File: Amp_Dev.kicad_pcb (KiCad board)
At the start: 2 copper layers, 100 x 100 mm, 511 parts, among them J1 SMA, J10 SMA, J11 CONN_01X02, J12 TEST_1P, J13 SMA, J14 CONN_01X02, J15 CONN_01X03, J16 TEST_1P, J17 TEST_1P, J18 TEST_1P, J2 SMA, J20 SMA, J21 SMA, J22 SMA, J3 TEST_1P, J4 TEST_1P, J5 CONN_01X03, J6 TEST_1P, J7 CONN_01X03, J8 TEST_1P, J9 TEST_1P, Q1 DMN2075U, U1 MML09211H, U2 RF6886, U3 LMV358, U4 SN74LVC1G17, U5 TLV702, U6 LTC2644, U7 RT9183

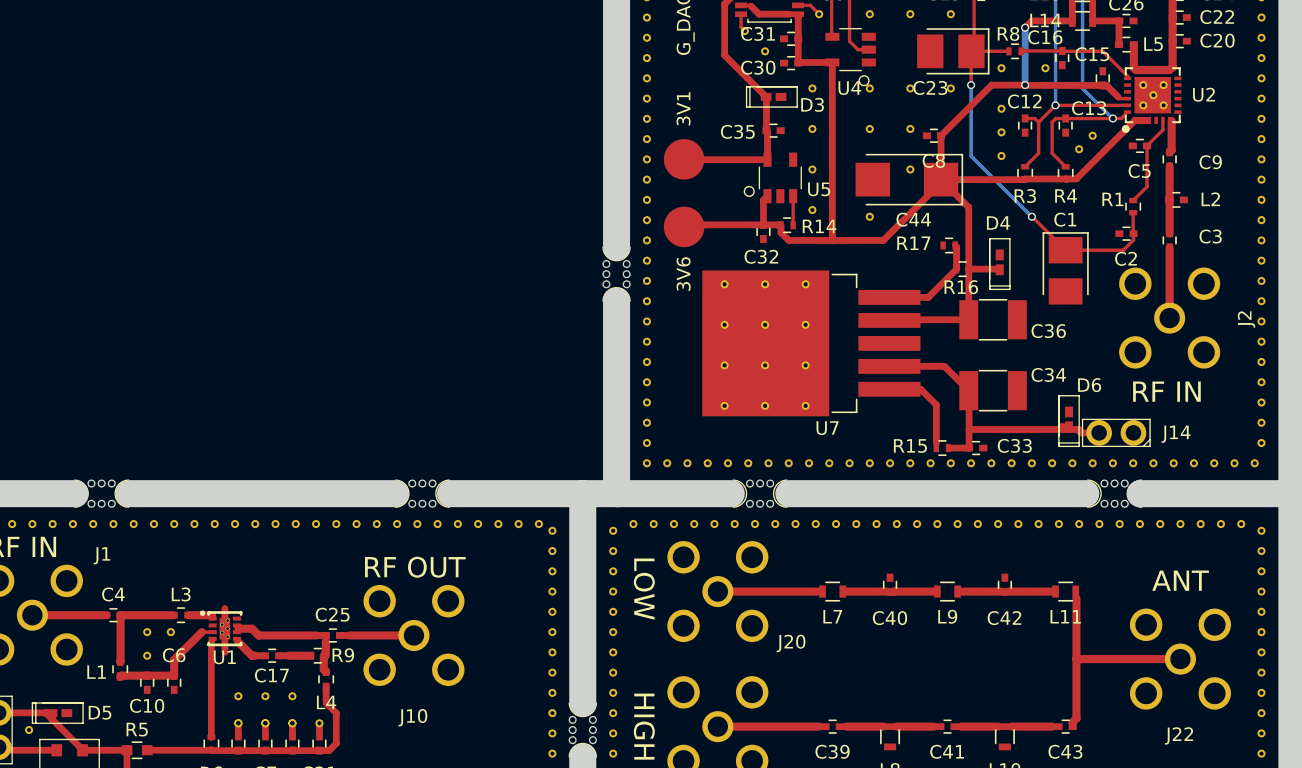
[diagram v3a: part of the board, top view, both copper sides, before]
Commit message: moved L1 closer to RF path
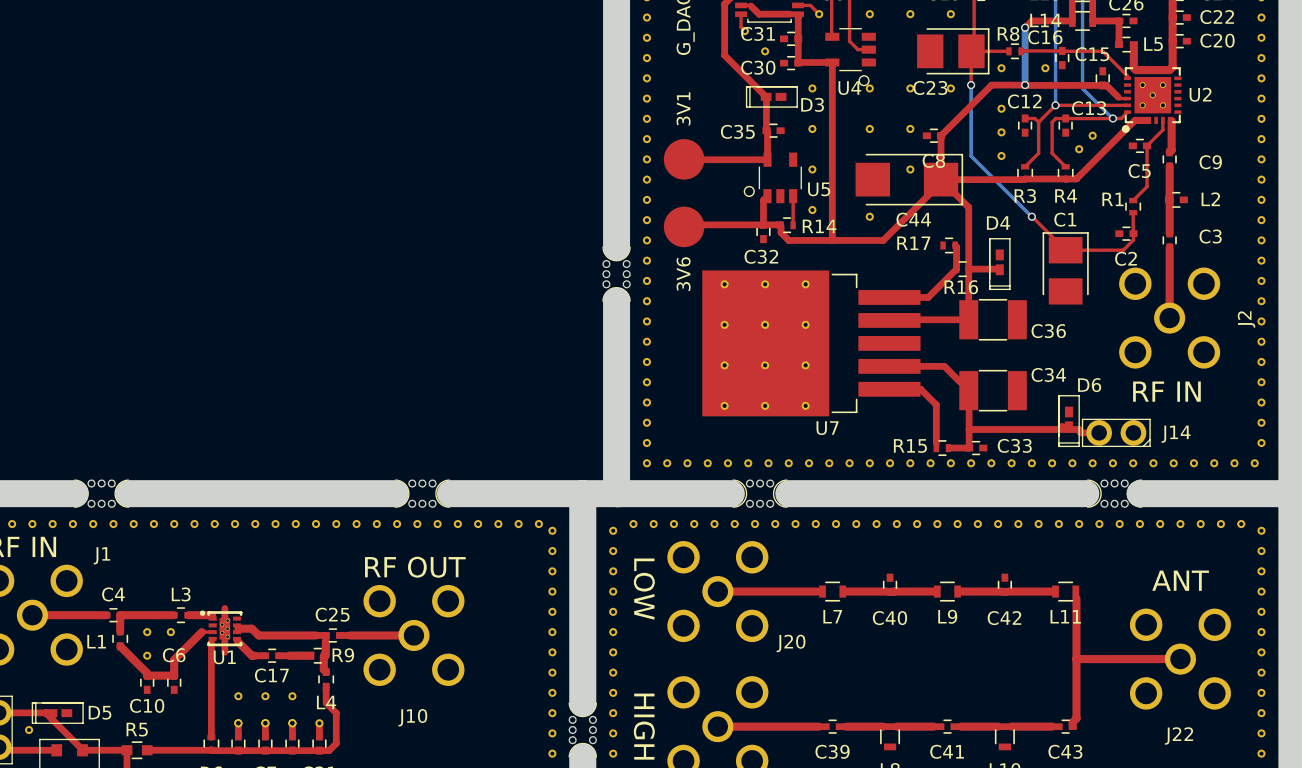
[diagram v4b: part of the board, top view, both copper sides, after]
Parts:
- removed the REF** at (189.0, 84.8)
- removed the REF** at (189.0, 86.2)
- removed the REF** at (190.5, 86.2)
- removed the REF** at (190.5, 84.8)
- removed the REF** at (189.8, 85.5)
- moved L1 2.25 mm to (113.2, 125.8)
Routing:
- net Net-(C4-Pad1): track 7.39 -> 5.14 mm
- net Net-(C10-Pad1): track 8.91 -> 9.88 mm

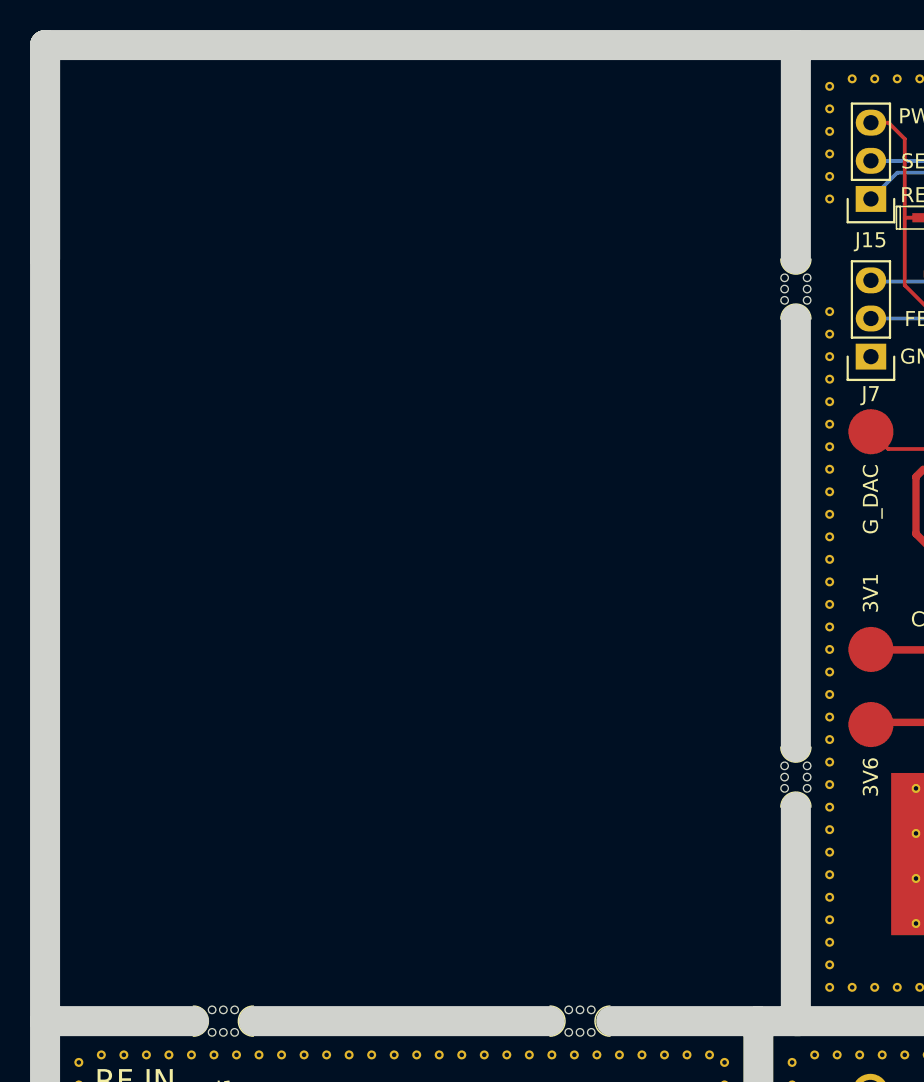
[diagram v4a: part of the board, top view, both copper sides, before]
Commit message: Duplicated PA board
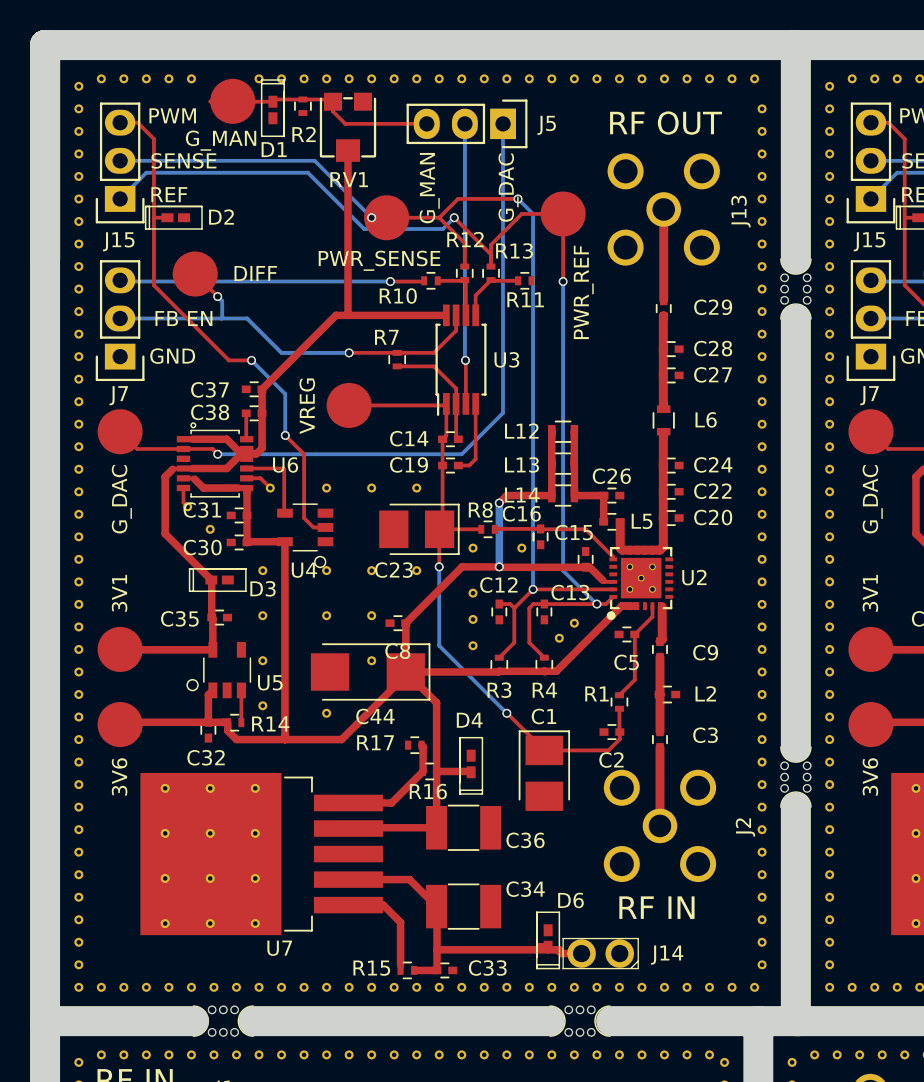
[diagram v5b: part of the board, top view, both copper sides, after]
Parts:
- added C1: 10uF, SFUSat:CP_Tantalum_Case-B_EIA-1411-21_Reflow, F.Cu at (133.2, 98.5)
- added C12: 1uF, SFUSat:C_0402, F.Cu at (130.2, 87.8)
- added C13: 1uF, SFUSat:C_0402, F.Cu at (133.2, 87.8)
- added C14: 0.1uF, SFUSat:C_0402, F.Cu at (127.0, 76.2)
- added C15: 1uF, SFUSat:C_0402, F.Cu at (136.0, 84.2)
- added C16: 2.2uF, SFUSat:C_0402, F.Cu at (133.0, 82.8)
- added C19: 1uF, SFUSat:C_0402, F.Cu at (127.0, 78.0)
- added C2: 1uF, SFUSat:C_0402, F.Cu at (137.8, 95.8)
- added C20: DNP, SFUSat:C_0402, F.Cu at (141.7, 81.5)
- added C22: 10pF, SFUSat:C_0402, F.Cu at (141.7, 79.8)
- added C23: 10uF, SFUSat:CP_Tantalum_Case-B_EIA-1411-21_Reflow, F.Cu at (124.8, 82.2)
- added C24: 27pF, SFUSat:C_0402, F.Cu at (141.7, 78.0)
- added C26: 2.2uF, SFUSat:C_0402, F.Cu at (137.8, 80.0)
- added C27: 10pF, SFUSat:C_0402, F.Cu at (141.7, 72.0)
- added C28: 1.2pF, SFUSat:C_0402, F.Cu at (141.7, 70.2)
- added C29: 100pF, SFUSat:C_0402, F.Cu at (141.2, 67.5)
- added C3: 100pF, SFUSat:C_0402, F.Cu at (140.9, 96.2)
- added C30: 0.1uF, SFUSat:C_0402, F.Cu at (112.9, 83.1)
- added C31: 0.1uF, SFUSat:C_0402, F.Cu at (112.9, 81.3)
- added C32: 1uF, SFUSat:C_0402, F.Cu at (110.9, 95.6)
- added C33: 0.1uF, SFUSat:C_0402, F.Cu at (126.6, 111.6)
- added C34: 10uF, SFUSat:C_1210, F.Cu at (127.9, 107.4)
- added C35: 1uF, SFUSat:C_0402, F.Cu at (111.6, 88.1)
- added C36: 10uF, SFUSat:C_1210, F.Cu at (127.9, 102.1)
- added C37: 0.1uF, SFUSat:C_0402, F.Cu at (113.9, 72.9)
- added C38: 0.1uF, SFUSat:C_0402, F.Cu at (113.9, 74.5)
- added C44: 10uF, SFUSat:CP_Tantalum_Case-C_EIA-2312-28_Reflow, F.Cu at (121.5, 91.8)
- added C5: 2.2uF, SFUSat:C_0402, F.Cu at (138.8, 89.2)
- added C8: 220pF, SFUSat:C_0402, F.Cu at (123.5, 88.5)
- added C9: 22pF, SFUSat:C_0402, F.Cu at (140.9, 90.2)
- added D1: PESD5Zx, SFUSat:PESD57zx, F.Cu at (115.2, 54.3)
- added D2: PESD5Zx, SFUSat:PESD57zx, F.Cu at (108.7, 61.5)
- added D3: PESD5Zx, SFUSat:PESD57zx, F.Cu at (111.6, 85.6)
- added D4: PESD5Zx, SFUSat:PESD57zx, F.Cu at (128.4, 97.9)
- added D6: PESD5Zx, SFUSat:PESD57zx, F.Cu at (133.5, 109.5)
- added G***: LOGO, SFUSat:SFUSat_15mm_2, B.Cu at (107.8, 105.8)
- added J13: SMA, SFUSat:SMA-Vert-TH, F.Cu at (141.2, 61.0)
- added J14: CONN_01X02, SFUSat:2x01In_Header_v2, F.Cu at (137.0, 110.5)
- added J15: CONN_01X03, SFUSat:Socket_Strip_Straight_1x03, F.Cu at (105.0, 60.2)
- added J16: TEST_1P, SFUSat:Measurement_Point_Round-SMD-Pad_Big, F.Cu at (105.0, 90.2)
- added J17: TEST_1P, SFUSat:Measurement_Point_Round-SMD-Pad_Big, F.Cu at (105.0, 95.2)
- added J18: TEST_1P, SFUSat:Measurement_Point_Round-SMD-Pad_Big, F.Cu at (105.0, 75.8)
- added J2: SMA, SFUSat:SMA-Vert-TH, F.Cu at (140.9, 102.0)
- added J3: TEST_1P, SFUSat:Measurement_Point_Round-SMD-Pad_Big, F.Cu at (112.5, 53.8)
- added J4: TEST_1P, SFUSat:Measurement_Point_Round-SMD-Pad_Big, F.Cu at (120.2, 74.0)
- added J5: CONN_01X03, SFUSat:Socket_Strip_Straight_1x03, F.Cu at (130.5, 55.2)
- added J6: TEST_1P, SFUSat:Measurement_Point_Round-SMD-Pad_Big, F.Cu at (110.0, 65.2)
- added J7: CONN_01X03, SFUSat:Socket_Strip_Straight_1x03, F.Cu at (105.0, 70.8)
- added J8: TEST_1P, SFUSat:Measurement_Point_Round-SMD-Pad_Big, F.Cu at (122.8, 61.5)
- added J9: TEST_1P, SFUSat:Measurement_Point_Round-SMD-Pad_Big, F.Cu at (134.5, 61.2)
- added L12: 0R0, SFUSat:L_0603, F.Cu at (134.5, 75.8)
- added L13: 0R0, SFUSat:L_0603, F.Cu at (134.5, 77.9)
- added L14: 0R0, SFUSat:L_0603, F.Cu at (134.5, 80.0)
- added L2: 8.2nH, SFUSat:L_0402, F.Cu at (141.4, 93.2)
- added L5: 12.55nH, SFUSat:L_0402, F.Cu at (137.8, 81.8)
- added L6: 0R0, SFUSat:L_0603, F.Cu at (141.2, 75.0)
- added R1: 220R, SFUSat:R_0402, F.Cu at (138.2, 93.8)
- added R10: 10K, SFUSat:R_0402, F.Cu at (125.7, 65.7)
- added R11: 10K, SFUSat:R_0402, F.Cu at (131.9, 65.7)
- added R12: 10K, SFUSat:R_0402, F.Cu at (128.0, 65.2)
- added R13: 10K, SFUSat:R_0402, F.Cu at (129.7, 65.2)
- added R14: 1K, SFUSat:R_0402, F.Cu at (112.6, 95.1)
- added R15: 1k, SFUSat:R_0402, F.Cu at (124.1, 111.6)
- added R16: 1k, SFUSat:R_0402, F.Cu at (125.6, 98.4)
- added R17: 287R, SFUSat:R_0402, F.Cu at (124.6, 96.6)
- added R2: 1K, SFUSat:R_0402, F.Cu at (117.2, 54.1)
- added R3: 390R, SFUSat:R_0402, F.Cu at (130.2, 91.2)
- added R4: 390R, SFUSat:R_0402, F.Cu at (133.2, 91.2)
- added R7: 1K, SFUSat:R_0402, F.Cu at (123.5, 71.0)
- added R8: 220R, SFUSat:R_0402, F.Cu at (129.5, 82.2)
- added REF**: VIA-0.6mm, SFUSat:VIA-0.6mm, F.Cu at (152.2, 66.2)
- added REF**: VIA-0.6mm, SFUSat:VIA-0.6mm, F.Cu at (115.0, 79.5)
- added REF**: VIA-0.6mm, SFUSat:VIA-0.6mm, F.Cu at (147.8, 78.2)
- added REF**: VIA-0.6mm, SFUSat:VIA-0.6mm, F.Cu at (147.8, 76.8)
- added REF**: VIA-0.6mm, SFUSat:VIA-0.6mm, F.Cu at (147.8, 75.2)
- added REF**: VIA-0.6mm, SFUSat:VIA-0.6mm, F.Cu at (147.8, 73.8)
- added REF**: VIA-0.6mm, SFUSat:VIA-0.6mm, F.Cu at (147.8, 72.2)
- added REF**: VIA-0.6mm, SFUSat:VIA-0.6mm, F.Cu at (147.8, 70.8)
- added REF**: VIA-0.6mm, SFUSat:VIA-0.6mm, F.Cu at (147.8, 69.2)
- added REF**: VIA-0.6mm, SFUSat:VIA-0.6mm, F.Cu at (147.8, 67.8)
- added REF**: VIA-0.6mm, SFUSat:VIA-0.6mm, F.Cu at (147.8, 66.2)
- added REF**: VIA-0.6mm, SFUSat:VIA-0.6mm, F.Cu at (147.8, 64.8)
- added REF**: VIA-0.6mm, SFUSat:VIA-0.6mm, F.Cu at (102.2, 112.8)
- added REF**: VIA-0.6mm, SFUSat:VIA-0.6mm, F.Cu at (147.8, 63.2)
- added REF**: VIA-0.6mm, SFUSat:VIA-0.6mm, F.Cu at (147.8, 61.8)
- added REF**: VIA-0.6mm, SFUSat:VIA-0.6mm, F.Cu at (147.8, 60.2)
- added REF**: VIA-0.6mm, SFUSat:VIA-0.6mm, F.Cu at (147.8, 58.8)
- added REF**: VIA-0.6mm, SFUSat:VIA-0.6mm, F.Cu at (147.8, 57.2)
- added REF**: VIA-0.6mm, SFUSat:VIA-0.6mm, F.Cu at (147.8, 55.8)
- added REF**: VIA-0.6mm, SFUSat:VIA-0.6mm, F.Cu at (147.8, 54.2)
- added REF**: VIA-0.6mm, SFUSat:VIA-0.6mm, F.Cu at (103.8, 52.2)
- added REF**: VIA-0.6mm, SFUSat:VIA-0.6mm, F.Cu at (105.2, 52.2)
- added REF**: VIA-0.6mm, SFUSat:VIA-0.6mm, F.Cu at (106.8, 52.2)
- added REF**: VIA-0.6mm, SFUSat:VIA-0.6mm, F.Cu at (102.2, 111.2)
- added REF**: VIA-0.6mm, SFUSat:VIA-0.6mm, F.Cu at (108.2, 52.2)
- added REF**: VIA-0.6mm, SFUSat:VIA-0.6mm, F.Cu at (109.8, 52.2)
- added REF**: VIA-0.6mm, SFUSat:VIA-0.6mm, F.Cu at (114.2, 52.2)
- added REF**: VIA-0.6mm, SFUSat:VIA-0.6mm, F.Cu at (115.8, 52.2)
- added REF**: VIA-0.6mm, SFUSat:VIA-0.6mm, F.Cu at (117.2, 52.2)
- added REF**: VIA-0.6mm, SFUSat:VIA-0.6mm, F.Cu at (118.8, 52.2)
- added REF**: VIA-0.6mm, SFUSat:VIA-0.6mm, F.Cu at (120.2, 52.2)
- added REF**: VIA-0.6mm, SFUSat:VIA-0.6mm, F.Cu at (121.8, 52.2)
- added REF**: VIA-0.6mm, SFUSat:VIA-0.6mm, F.Cu at (123.2, 52.2)
- added REF**: VIA-0.6mm, SFUSat:VIA-0.6mm, F.Cu at (124.8, 52.2)
- added REF**: VIA-0.6mm, SFUSat:VIA-0.6mm, F.Cu at (102.2, 109.8)
- added REF**: VIA-0.6mm, SFUSat:VIA-0.6mm, F.Cu at (126.2, 52.2)
- added REF**: VIA-0.6mm, SFUSat:VIA-0.6mm, F.Cu at (127.8, 52.2)
- added REF**: VIA-0.6mm, SFUSat:VIA-0.6mm, F.Cu at (129.2, 52.2)
- added REF**: VIA-0.6mm, SFUSat:VIA-0.6mm, F.Cu at (130.8, 52.2)
- added REF**: VIA-0.6mm, SFUSat:VIA-0.6mm, F.Cu at (132.2, 52.2)
- added REF**: VIA-0.6mm, SFUSat:VIA-0.6mm, F.Cu at (133.8, 52.2)
- added REF**: VIA-0.6mm, SFUSat:VIA-0.6mm, F.Cu at (135.2, 52.2)
- added REF**: VIA-0.6mm, SFUSat:VIA-0.6mm, F.Cu at (136.8, 52.2)
- added REF**: VIA-0.6mm, SFUSat:VIA-0.6mm, F.Cu at (138.2, 52.2)
- added REF**: VIA-0.6mm, SFUSat:VIA-0.6mm, F.Cu at (139.8, 52.2)
- added REF**: VIA-0.6mm, SFUSat:VIA-0.6mm, F.Cu at (102.2, 108.2)
- added REF**: VIA-0.6mm, SFUSat:VIA-0.6mm, F.Cu at (141.2, 52.2)
- added REF**: VIA-0.6mm, SFUSat:VIA-0.6mm, F.Cu at (142.8, 52.2)
- added REF**: VIA-0.6mm, SFUSat:VIA-0.6mm, F.Cu at (144.2, 52.2)
- added REF**: VIA-0.6mm, SFUSat:VIA-0.6mm, F.Cu at (145.8, 52.2)
- added REF**: VIA-0.6mm, SFUSat:VIA-0.6mm, F.Cu at (147.2, 52.2)
- added REF**: VIA-0.6mm, SFUSat:VIA-0.6mm, F.Cu at (128.5, 90.0)
- added REF**: VIA-0.6mm, SFUSat:VIA-0.6mm, F.Cu at (128.5, 88.2)
- added REF**: VIA-0.6mm, SFUSat:VIA-0.6mm, F.Cu at (128.5, 86.5)
- added REF**: VIA-0.6mm, SFUSat:VIA-0.6mm, F.Cu at (134.2, 89.5)
- added REF**: VIA-0.6mm, SFUSat:VIA-0.6mm, F.Cu at (128.5, 83.5)
- added REF**: VIA-0.6mm, SFUSat:VIA-0.6mm, F.Cu at (102.2, 106.8)
- added REF**: VIA-0.6mm, SFUSat:VIA-0.6mm, F.Cu at (131.8, 83.5)
- added REF**: VIA-0.6mm, SFUSat:VIA-0.6mm, F.Cu at (108.0, 99.5)
- added REF**: VIA-0.6mm, SFUSat:VIA-0.6mm, F.Cu at (111.0, 99.5)
- added REF**: VIA-0.6mm, SFUSat:VIA-0.6mm, F.Cu at (114.0, 99.5)
- added REF**: VIA-0.6mm, SFUSat:VIA-0.6mm, F.Cu at (108.0, 102.5)
- added REF**: VIA-0.6mm, SFUSat:VIA-0.6mm, F.Cu at (111.0, 102.5)
- added REF**: VIA-0.6mm, SFUSat:VIA-0.6mm, F.Cu at (114.0, 102.5)
- added REF**: VIA-0.6mm, SFUSat:VIA-0.6mm, F.Cu at (108.0, 105.5)
- added REF**: VIA-0.6mm, SFUSat:VIA-0.6mm, F.Cu at (111.0, 105.5)
- added REF**: VIA-0.6mm, SFUSat:VIA-0.6mm, F.Cu at (114.0, 105.5)
- added REF**: VIA-0.6mm, SFUSat:VIA-0.6mm, F.Cu at (102.2, 105.2)
- added REF**: VIA-0.6mm, SFUSat:VIA-0.6mm, F.Cu at (108.0, 108.5)
- added REF**: VIA-0.6mm, SFUSat:VIA-0.6mm, F.Cu at (111.0, 108.5)
- added REF**: VIA-0.6mm, SFUSat:VIA-0.6mm, F.Cu at (114.0, 108.5)
- added REF**: VIA-0.6mm, SFUSat:VIA-0.6mm, F.Cu at (109.5, 80.8)
- added REF**: VIA-0.6mm, SFUSat:VIA-0.6mm, F.Cu at (118.8, 79.5)
- added REF**: VIA-0.6mm, SFUSat:VIA-0.6mm, F.Cu at (121.8, 79.5)
- added REF**: VIA-0.6mm, SFUSat:VIA-0.6mm, F.Cu at (124.8, 79.5)
- added REF**: VIA-0.6mm, SFUSat:VIA-0.6mm, F.Cu at (118.8, 85.0)
- added REF**: VIA-0.6mm, SFUSat:VIA-0.6mm, F.Cu at (124.8, 85.0)
- added REF**: VIA-0.6mm, SFUSat:VIA-0.6mm, F.Cu at (121.8, 85.0)
- added REF**: VIA-0.6mm, SFUSat:VIA-0.6mm, F.Cu at (102.2, 103.8)
- added REF**: VIA-0.6mm, SFUSat:VIA-0.6mm, F.Cu at (118.8, 88.0)
- added REF**: VIA-0.6mm, SFUSat:VIA-0.6mm, F.Cu at (121.8, 88.0)
- added REF**: VIA-0.6mm, SFUSat:VIA-0.6mm, F.Cu at (118.8, 94.5)
- added REF**: VIA-0.6mm, SFUSat:VIA-0.6mm, F.Cu at (121.8, 91.0)
- added REF**: VIA-0.6mm, SFUSat:VIA-0.6mm, F.Cu at (111.0, 82.2)
- added REF**: VIA-0.6mm, SFUSat:VIA-0.6mm, F.Cu at (114.5, 85.0)
- added REF**: VIA-0.6mm, SFUSat:VIA-0.6mm, F.Cu at (114.5, 88.0)
- added REF**: VIA-0.6mm, SFUSat:VIA-0.6mm, F.Cu at (114.5, 91.0)
- added REF**: VIA-0.6mm, SFUSat:VIA-0.6mm, F.Cu at (114.5, 94.0)
- added REF**: VIA-0.6mm, SFUSat:VIA-0.6mm, F.Cu at (102.2, 102.2)
- added REF**: VIA-0.6mm, SFUSat:VIA-0.6mm, F.Cu at (102.2, 100.8)
- added REF**: VIA-0.6mm, SFUSat:VIA-0.6mm, F.Cu at (152.2, 64.8)
- added REF**: VIA-0.6mm, SFUSat:VIA-0.6mm, F.Cu at (102.2, 99.2)
- added REF**: VIA-0.6mm, SFUSat:VIA-0.6mm, F.Cu at (102.2, 97.8)
- added REF**: VIA-0.6mm, SFUSat:VIA-0.6mm, F.Cu at (102.2, 96.2)
- added REF**: VIA-0.6mm, SFUSat:VIA-0.6mm, F.Cu at (102.2, 94.8)
- added REF**: VIA-0.6mm, SFUSat:VIA-0.6mm, F.Cu at (102.2, 93.2)
- added REF**: VIA-0.6mm, SFUSat:VIA-0.6mm, F.Cu at (102.2, 91.8)
- added REF**: VIA-0.6mm, SFUSat:VIA-0.6mm, F.Cu at (102.2, 90.2)
- added REF**: VIA-0.6mm, SFUSat:VIA-0.6mm, F.Cu at (102.2, 88.8)
- added REF**: VIA-0.6mm, SFUSat:VIA-0.6mm, F.Cu at (102.2, 87.2)
- added REF**: VIA-0.6mm, SFUSat:VIA-0.6mm, F.Cu at (102.2, 85.8)
- added REF**: VIA-0.6mm, SFUSat:VIA-0.6mm, F.Cu at (152.2, 63.2)
- added REF**: VIA-0.6mm, SFUSat:VIA-0.6mm, F.Cu at (102.2, 84.2)
- added REF**: VIA-0.6mm, SFUSat:VIA-0.6mm, F.Cu at (102.2, 82.8)
- added REF**: VIA-0.6mm, SFUSat:VIA-0.6mm, F.Cu at (102.2, 81.2)
- added REF**: VIA-0.6mm, SFUSat:VIA-0.6mm, F.Cu at (102.2, 79.8)
- added REF**: VIA-0.6mm, SFUSat:VIA-0.6mm, F.Cu at (102.2, 78.2)
- added REF**: VIA-0.6mm, SFUSat:VIA-0.6mm, F.Cu at (102.2, 76.8)
- added REF**: VIA-0.6mm, SFUSat:VIA-0.6mm, F.Cu at (102.2, 75.2)
- added REF**: VIA-0.6mm, SFUSat:VIA-0.6mm, F.Cu at (102.2, 73.8)
- added REF**: VIA-0.6mm, SFUSat:VIA-0.6mm, F.Cu at (102.2, 72.2)
- added REF**: VIA-0.6mm, SFUSat:VIA-0.6mm, F.Cu at (102.2, 70.8)
- added REF**: VIA-0.6mm, SFUSat:VIA-0.6mm, F.Cu at (152.2, 61.8)
- added REF**: VIA-0.6mm, SFUSat:VIA-0.6mm, F.Cu at (102.2, 69.2)
- added REF**: VIA-0.6mm, SFUSat:VIA-0.6mm, F.Cu at (102.2, 67.8)
- added REF**: VIA-0.6mm, SFUSat:VIA-0.6mm, F.Cu at (102.2, 60.2)
- added REF**: VIA-0.6mm, SFUSat:VIA-0.6mm, F.Cu at (102.2, 58.8)
- added REF**: VIA-0.6mm, SFUSat:VIA-0.6mm, F.Cu at (102.2, 57.2)
- added REF**: VIA-0.6mm, SFUSat:VIA-0.6mm, F.Cu at (102.2, 55.8)
- added REF**: VIA-0.6mm, SFUSat:VIA-0.6mm, F.Cu at (102.2, 54.2)
- added REF**: VIA-0.6mm, SFUSat:VIA-0.6mm, F.Cu at (102.2, 52.8)
- added REF**: VIA-0.6mm, SFUSat:VIA-0.6mm, F.Cu at (103.8, 112.8)
- added REF**: VIA-0.6mm, SFUSat:VIA-0.6mm, F.Cu at (105.2, 112.8)
- added REF**: VIA-0.6mm, SFUSat:VIA-0.6mm, F.Cu at (102.2, 66.2)
- added REF**: VIA-0.6mm, SFUSat:VIA-0.6mm, F.Cu at (106.8, 112.8)
- added REF**: VIA-0.6mm, SFUSat:VIA-0.6mm, F.Cu at (108.2, 112.8)
- added REF**: VIA-0.6mm, SFUSat:VIA-0.6mm, F.Cu at (109.8, 112.8)
- added REF**: VIA-0.6mm, SFUSat:VIA-0.6mm, F.Cu at (111.2, 112.8)
- added REF**: VIA-0.6mm, SFUSat:VIA-0.6mm, F.Cu at (112.8, 112.8)
- added REF**: VIA-0.6mm, SFUSat:VIA-0.6mm, F.Cu at (114.2, 112.8)
- added REF**: VIA-0.6mm, SFUSat:VIA-0.6mm, F.Cu at (115.8, 112.8)
- added REF**: VIA-0.6mm, SFUSat:VIA-0.6mm, F.Cu at (117.2, 112.8)
- added REF**: VIA-0.6mm, SFUSat:VIA-0.6mm, F.Cu at (118.8, 112.8)
- added REF**: VIA-0.6mm, SFUSat:VIA-0.6mm, F.Cu at (120.2, 112.8)
- added REF**: VIA-0.6mm, SFUSat:VIA-0.6mm, F.Cu at (102.2, 64.8)
- added REF**: VIA-0.6mm, SFUSat:VIA-0.6mm, F.Cu at (121.8, 112.8)
- added REF**: VIA-0.6mm, SFUSat:VIA-0.6mm, F.Cu at (123.2, 112.8)
- added REF**: VIA-0.6mm, SFUSat:VIA-0.6mm, F.Cu at (124.8, 112.8)
- added REF**: VIA-0.6mm, SFUSat:VIA-0.6mm, F.Cu at (126.2, 112.8)
- added REF**: VIA-0.6mm, SFUSat:VIA-0.6mm, F.Cu at (127.8, 112.8)
- added REF**: VIA-0.6mm, SFUSat:VIA-0.6mm, F.Cu at (129.2, 112.8)
- added REF**: VIA-0.6mm, SFUSat:VIA-0.6mm, F.Cu at (130.8, 112.8)
- added REF**: VIA-0.6mm, SFUSat:VIA-0.6mm, F.Cu at (132.2, 112.8)
- added REF**: VIA-0.6mm, SFUSat:VIA-0.6mm, F.Cu at (133.8, 112.8)
- added REF**: VIA-0.6mm, SFUSat:VIA-0.6mm, F.Cu at (135.2, 112.8)
- added REF**: VIA-0.6mm, SFUSat:VIA-0.6mm, F.Cu at (102.2, 63.2)
- added REF**: VIA-0.6mm, SFUSat:VIA-0.6mm, F.Cu at (136.8, 112.8)
- added REF**: VIA-0.6mm, SFUSat:VIA-0.6mm, F.Cu at (138.2, 112.8)
- added REF**: VIA-0.6mm, SFUSat:VIA-0.6mm, F.Cu at (139.8, 112.8)
- added REF**: VIA-0.6mm, SFUSat:VIA-0.6mm, F.Cu at (141.2, 112.8)
- added REF**: VIA-0.6mm, SFUSat:VIA-0.6mm, F.Cu at (142.8, 112.8)
- added REF**: VIA-0.6mm, SFUSat:VIA-0.6mm, F.Cu at (144.2, 112.8)
- added REF**: VIA-0.6mm, SFUSat:VIA-0.6mm, F.Cu at (145.8, 112.8)
- added REF**: VIA-0.6mm, SFUSat:VIA-0.6mm, F.Cu at (147.2, 112.8)
- added REF**: VIA-0.6mm, SFUSat:VIA-0.6mm, F.Cu at (147.8, 111.2)
- added REF**: VIA-0.6mm, SFUSat:VIA-0.6mm, F.Cu at (147.8, 109.8)
- added REF**: VIA-0.6mm, SFUSat:VIA-0.6mm, F.Cu at (102.2, 61.8)
- added REF**: VIA-0.6mm, SFUSat:VIA-0.6mm, F.Cu at (147.8, 108.2)
- added REF**: VIA-0.6mm, SFUSat:VIA-0.6mm, F.Cu at (147.8, 106.8)
- added REF**: VIA-0.6mm, SFUSat:VIA-0.6mm, F.Cu at (147.8, 105.2)
- added REF**: VIA-0.6mm, SFUSat:VIA-0.6mm, F.Cu at (147.8, 103.8)
- added REF**: VIA-0.6mm, SFUSat:VIA-0.6mm, F.Cu at (147.8, 102.2)
- added REF**: VIA-0.6mm, SFUSat:VIA-0.6mm, F.Cu at (147.8, 100.8)
- added REF**: VIA-0.6mm, SFUSat:VIA-0.6mm, F.Cu at (147.8, 99.2)
- added REF**: VIA-0.6mm, SFUSat:VIA-0.6mm, F.Cu at (147.8, 97.8)
- added REF**: VIA-0.6mm, SFUSat:VIA-0.6mm, F.Cu at (147.8, 96.2)
- added REF**: VIA-0.6mm, SFUSat:VIA-0.6mm, F.Cu at (147.8, 94.8)
- added REF**: VIA-0.6mm, SFUSat:VIA-0.6mm, F.Cu at (135.2, 88.5)
- added REF**: VIA-0.6mm, SFUSat:VIA-0.6mm, F.Cu at (147.8, 93.2)
- added REF**: VIA-0.6mm, SFUSat:VIA-0.6mm, F.Cu at (147.8, 91.8)
- added REF**: VIA-0.6mm, SFUSat:VIA-0.6mm, F.Cu at (147.8, 90.2)
- added REF**: VIA-0.6mm, SFUSat:VIA-0.6mm, F.Cu at (147.8, 88.8)
- added REF**: VIA-0.6mm, SFUSat:VIA-0.6mm, F.Cu at (147.8, 87.2)
- added REF**: VIA-0.6mm, SFUSat:VIA-0.6mm, F.Cu at (147.8, 85.8)
- added REF**: VIA-0.6mm, SFUSat:VIA-0.6mm, F.Cu at (147.8, 84.2)
- added REF**: VIA-0.6mm, SFUSat:VIA-0.6mm, F.Cu at (147.8, 82.8)
- added REF**: VIA-0.6mm, SFUSat:VIA-0.6mm, F.Cu at (147.8, 81.2)
- added REF**: VIA-0.6mm, SFUSat:VIA-0.6mm, F.Cu at (147.8, 79.8)
- added RV1: POT, SFUSat:TC33_SMD, F.Cu at (120.2, 55.6)
- added U2: RF6886, SFUSat:QFN-24, F.Cu at (139.7, 85.5)
- added U3: LMV358, SFUSat:TSSOP-8_4.4x3mm_Pitch0.65mm, F.Cu at (127.7, 71.0)
- added U4: SN74LVC1G17, SFUSat:SOT_23_5, F.Cu at (117.3, 82.1)
- added U5: TLV702, SFUSat:SOT_23_5, F.Cu at (112.1, 91.6)
- added U6: LTC2644, SFUSat:12-TSSOP, F.Cu at (111.3, 77.9)
- added U7: RT9183, SFUSat:TO-263-5Lead, F.Cu at (115.6, 103.9)
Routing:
- net /3V6: track 117.1 -> 234.1 mm, vias 2 -> 4
- net /PWR_REF: track 72.8 -> 145.5 mm, vias 3 -> 6
- net /PWR_SENSE: track 70.9 -> 141.8 mm, vias 3 -> 6
- net /3V1: track 60.7 -> 121.3 mm
- net /G_DAC: track 46.5 -> 93.0 mm, vias 1 -> 2
- net /VREG: track 42.9 -> 85.8 mm, vias 2 -> 4
- net /MCU_PWM: track 35.6 -> 71.1 mm, vias 2 -> 4
- net Net-(J6-Pad1): track 29.5 -> 59.0 mm, vias 2 -> 4
- net Net-(C33-Pad1): track 23.7 -> 47.3 mm
- net Net-(J7-Pad3): track 20.3 -> 40.6 mm, vias 1 -> 2
- net Net-(J5-Pad2): track 18.7 -> 37.4 mm, vias 1 -> 2
- net /G_MAN: track 15.5 -> 31.1 mm
- net Net-(C20-Pad1): track 12.5 -> 24.9 mm
- net GND: track 17.1 -> 27.0 mm
- net Net-(C16-Pad1): track 8.87 -> 17.7 mm
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
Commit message: generated and reviewed gerbers
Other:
- rule pad_to_mask_clearance: 0.2 -> 0

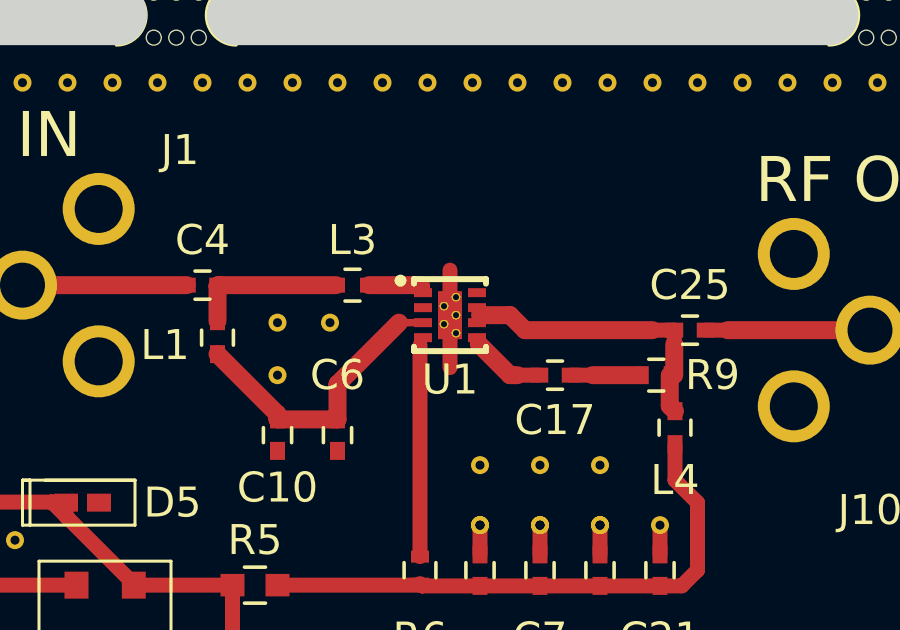
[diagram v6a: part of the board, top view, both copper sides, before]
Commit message: updated LNA footprint to one with 0.3mm drill
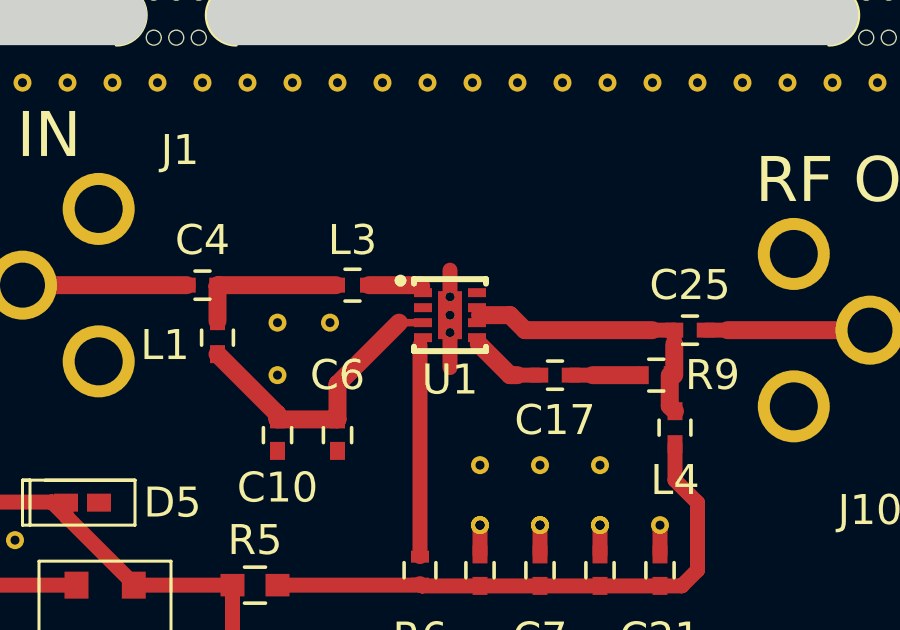
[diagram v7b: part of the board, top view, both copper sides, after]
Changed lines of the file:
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@@
 (kicad_pcb (version 4) (host pcbnew 4.0.6-e0-6349~53~ubuntu16.04.1)
   (general
-    (links 1029)
+    (links 1027)
     (no_connects 44)
     (area 84.435716 48.999999 202.188095 159.700001)
@@
       (net 4 GND) (zone_connect 2))
   )
-  (module SFUSat:8-VFDFN (layer F.Cu)
-    (at 121 125)
-    (fp_text reference U1 (at 0 2.15) (layer F.SilkS)
-      (effects (font (size 1 1) (thickness 0.15)))
-    )
-    (fp_text value MML09211H (at 0 -2) (layer F.Fab)
-      (effects (font (size 1 1) (thickness 0.15)))
-    )
-    (fp_circle (center -1.65 -1.15) (end -1.55 -1.15) (layer F.SilkS) (width 0.2))
-    (fp_line (start -1.2 1.2) (end -1.2 1.05) (layer F.SilkS) (width 0.2))
-    (fp_line (start 1.2 1.2) (end 1.2 1.05) (layer F.SilkS) (width 0.2))
-    (fp_line (start -1.2 1.2) (end 1.15 1.2) (layer F.SilkS) (width 0.2))
-    (fp_line (start 1.15 1.2) (end 1.2 1.2) (layer F.SilkS) (width 0.2))
-    (fp_line (start -1.2 -1.2) (end -1.2 -1.05) (layer F.SilkS) (width 0.2))
-    (fp_line (start -1.2 -1.2) (end 1.2 -1.2) (layer F.SilkS) (width 0.2))
-    (fp_line (start 1.2 -1.2) (end 1.2 -1.05) (layer F.SilkS) (width 0.2))
-    (fp_line (start -1 -1) (end 1 -1) (layer F.Fab) (width 0.2))
-    (fp_line (start 1 -1) (end 1 1) (layer F.Fab) (width 0.2))
-    (fp_line (start 1 1) (end -1 1) (layer F.Fab) (width 0.2))
-    (fp_line (start -1 1) (end -1 -1) (layer F.Fab) (width 0.2))
-    (pad 9 thru_hole circle (at 0.2 -0.6) (size 0.3 0.3) (drill 0.2) (layers *.Cu F.Mask)
-      (net 4 GND) (zone_connect 2))
-    (pad 9 thru_hole circle (at -0.2 -0.3) (size 0.3 0.3) (drill 0.2) (layers *.Cu F.Mask)
-      (net 4 GND) (zone_connect 2))
-    (pad 9 thru_hole circle (at -0.2 0.3) (size 0.3 0.3) (drill 0.2) (layers *.Cu F.Mask)
-      (net 4 GND) (zone_connect 2))
-    (pad 9 thru_hole circle (at 0.2 0.6) (size 0.3 0.3) (drill 0.2) (layers *.Cu F.Mask)
-      (net 4 GND) (zone_connect 2))
-    (pad 9 thru_hole circle (at 0.2 0) (size 0.3 0.3) (drill 0.2) (layers *.Cu F.Mask)
-      (net 4 GND) (zone_connect 2))
-    (pad 1 smd rect (at -0.9 -0.75) (size 0.6 0.3) (layers F.Cu F.Paste F.Mask)
-      (net 12 "Net-(L3-Pad1)"))
-    (pad 2 smd rect (at -0.9 -0.25) (size 0.6 0.3) (layers F.Cu F.Paste F.Mask)
-      (net 14 "Net-(U1-Pad2)"))
-    (pad 3 smd rect (at -0.9 0.25) (size 0.6 0.3) (layers F.Cu F.Paste F.Mask)
-      (net 3 "Net-(C10-Pad1)"))
-    (pad 4 smd rect (at -0.9 0.75) (size 0.6 0.3) (layers F.Cu F.Paste F.Mask)
-      (net 13 "Net-(R6-Pad2)"))
-    (pad 5 smd rect (at 0.9 0.75) (size 0.6 0.3) (layers F.Cu F.Paste F.Mask)
-      (net 7 "Net-(C17-Pad2)"))
-    (pad 6 smd rect (at 0.9 0.25) (size 0.6 0.3) (layers F.Cu F.Paste F.Mask)
-      (net 9 "Net-(C25-Pad2)"))
-    (pad 7 smd rect (at 0.9 -0.25) (size 0.6 0.3) (layers F.Cu F.Paste F.Mask)
-      (net 9 "Net-(C25-Pad2)"))
-    (pad 8 smd rect (at 0.9 -0.75) (size 0.6 0.3) (layers F.Cu F.Paste F.Mask)
-      (net 15 "Net-(U1-Pad8)"))
-    (pad 9 smd rect (at 0 0) (size 0.8 1.6) (layers F.Cu F.Paste F.Mask)
-      (net 4 GND))
-  )
   (module SFUSat:SFUSat_15mm_2 (layer F.Cu)
     (at 107 143)
@@
       (net 4 GND))
   )
+  (module SFUSat:8-VFDFN (layer F.Cu)
+    (at 121 125)
+    (fp_text reference U1 (at 0 2.15) (layer F.SilkS)
+      (effects (font (size 1 1) (thickness 0.15)))
+    )
+    (fp_text value MML09211H (at 0 -2) (layer F.Fab)
+      (effects (font (size 1 1) (thickness 0.15)))
+    )
+    (fp_circle (center -1.65 -1.15) (end -1.55 -1.15) (layer F.SilkS) (width 0.2))
+    (fp_line (start -1.2 1.2) (end -1.2 1.05) (layer F.SilkS) (width 0.2))
+    (fp_line (start 1.2 1.2) (end 1.2 1.05) (layer F.SilkS) (width 0.2))
+    (fp_line (start -1.2 1.2) (end 1.15 1.2) (layer F.SilkS) (width 0.2))
+    (fp_line (start 1.15 1.2) (end 1.2 1.2) (layer F.SilkS) (width 0.2))
+    (fp_line (start -1.2 -1.2) (end -1.2 -1.05) (layer F.SilkS) (width 0.2))
+    (fp_line (start -1.2 -1.2) (end 1.2 -1.2) (layer F.SilkS) (width 0.2))
+    (fp_line (start 1.2 -1.2) (end 1.2 -1.05) (layer F.SilkS) (width 0.2))
+    (fp_line (start -1 -1) (end 1 -1) (layer F.Fab) (width 0.2))
+    (fp_line (start 1 -1) (end 1 1) (layer F.Fab) (width 0.2))
+    (fp_line (start 1 1) (end -1 1) (layer F.Fab) (width 0.2))
+    (fp_line (start -1 1) (end -1 -1) (layer F.Fab) (width 0.2))
+    (pad 9 thru_hole circle (at 0 -0.61) (size 0.3 0.3) (drill 0.3) (layers *.Cu F.Mask)
+      (net 4 GND) (zone_connect 2))
+    (pad 9 thru_hole circle (at 0 0) (size 0.3 0.3) (drill 0.3) (layers *.Cu F.Mask)
+      (net 4 GND) (zone_connect 2))
+    (pad 9 thru_hole circle (at 0 0.58) (size 0.3 0.3) (drill 0.3) (layers *.Cu F.Mask)
+      (net 4 GND) (zone_connect 2))
+    (pad 1 smd rect (at -0.9 -0.75) (size 0.6 0.3) (layers F.Cu F.Paste F.Mask)
+      (net 12 "Net-(L3-Pad1)"))
+    (pad 2 smd rect (at -0.9 -0.25) (size 0.6 0.3) (layers F.Cu F.Paste F.Mask)
+      (net 14 "Net-(U1-Pad2)"))
+    (pad 3 smd rect (at -0.9 0.25) (size 0.6 0.3) (layers F.Cu F.Paste F.Mask)
+      (net 3 "Net-(C10-Pad1)"))
+    (pad 4 smd rect (at -0.9 0.75) (size 0.6 0.3) (layers F.Cu F.Paste F.Mask)
+      (net 13 "Net-(R6-Pad2)"))
+    (pad 5 smd rect (at 0.9 0.75) (size 0.6 0.3) (layers F.Cu F.Paste F.Mask)
+      (net 7 "Net-(C17-Pad2)"))
+    (pad 6 smd rect (at 0.9 0.25) (size 0.6 0.3) (layers F.Cu F.Paste F.Mask)
+      (net 9 "Net-(C25-Pad2)"))
+    (pad 7 smd rect (at 0.9 -0.25) (size 0.6 0.3) (layers F.Cu F.Paste F.Mask)
+      (net 9 "Net-(C25-Pad2)"))
+    (pad 8 smd rect (at 0.9 -0.75) (size 0.6 0.3) (layers F.Cu F.Paste F.Mask)
+      (net 15 "Net-(U1-Pad8)"))
+    (pad 9 smd rect (at 0 0) (size 0.8 1.6) (layers F.Cu F.Paste F.Mask)
+      (net 4 GND))
+  )
